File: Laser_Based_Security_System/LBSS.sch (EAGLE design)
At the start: 23 parts, among them IC1 7805TV

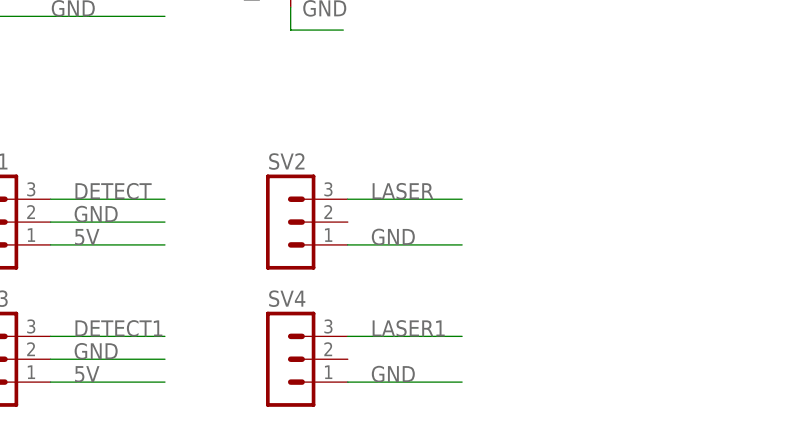
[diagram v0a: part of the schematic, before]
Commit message: Added Schematic
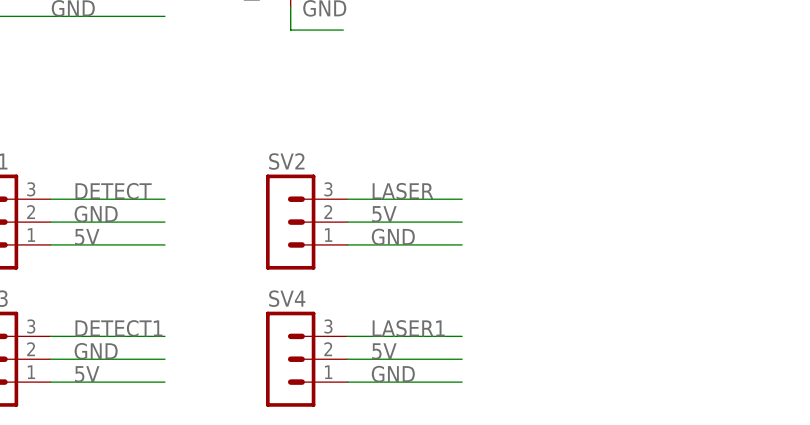
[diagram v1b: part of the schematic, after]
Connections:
- net 5V: now also SV2.2, SV4.2
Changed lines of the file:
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@@
 <label x="43.18" y="50.8" size="1.778" layer="95"/>
+</segment>
+<segment>
+<pinref part="SV2" gate="G$1" pin="2"/>
+<wire x1="73.66" y1="68.58" x2="86.36" y2="68.58" width="0.1524" layer="91"/>
+<label x="76.2" y="68.58" size="1.778" layer="95"/>
+</segment>
+<segment>
+<pinref part="SV4" gate="G$1" pin="2"/>
+<wire x1="73.66" y1="53.34" x2="86.36" y2="53.34" width="0.1524" layer="91"/>
+<label x="76.2" y="53.34" size="1.778" layer="95"/>
 </segment>
 </net>
